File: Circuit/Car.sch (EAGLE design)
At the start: 16 parts, among them M1 MOTOR, M2 MOTOR, U1 AMS1117-3.3, X2 ESP-12

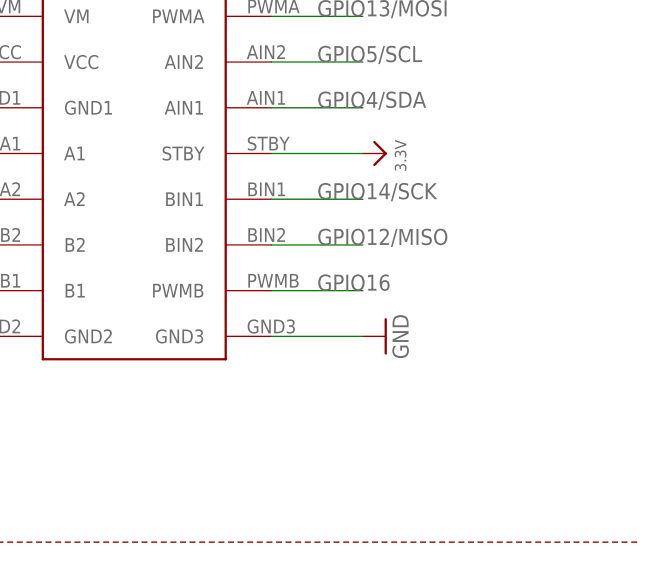
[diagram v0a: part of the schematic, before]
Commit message: Use one output for both pwms
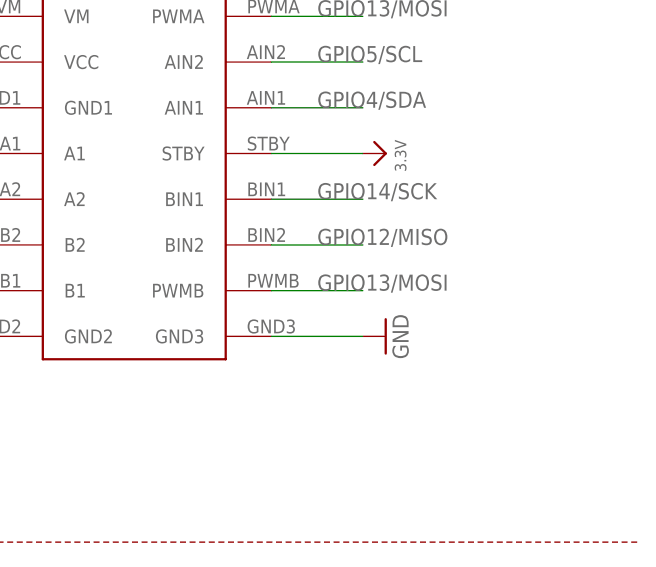
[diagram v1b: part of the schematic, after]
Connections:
- net GPIO13/MOSI: now also TB1.PWMB
- net GPIO16: no longer TB1.PWMB
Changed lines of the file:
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@@
 <label x="15.24" y="81.28" size="1.778" layer="95"/>
-</segment>
-<segment>
-<pinref part="TB1" gate="G$1" pin="PWMB"/>
-<wire x1="215.9" y1="124.46" x2="226.06" y2="124.46" width="0.1524" layer="91"/>
-<label x="220.98" y="124.46" size="1.778" layer="95"/>
 </segment>
 </net>
@@
 <label x="220.98" y="154.94" size="1.778" layer="95"/>
 </segment>
+<segment>
+<pinref part="TB1" gate="G$1" pin="PWMB"/>
+<wire x1="215.9" y1="124.46" x2="226.06" y2="124.46" width="0.1524" layer="91"/>
+<label x="220.98" y="124.46" size="1.778" layer="95"/>
+</segment>
 </net>

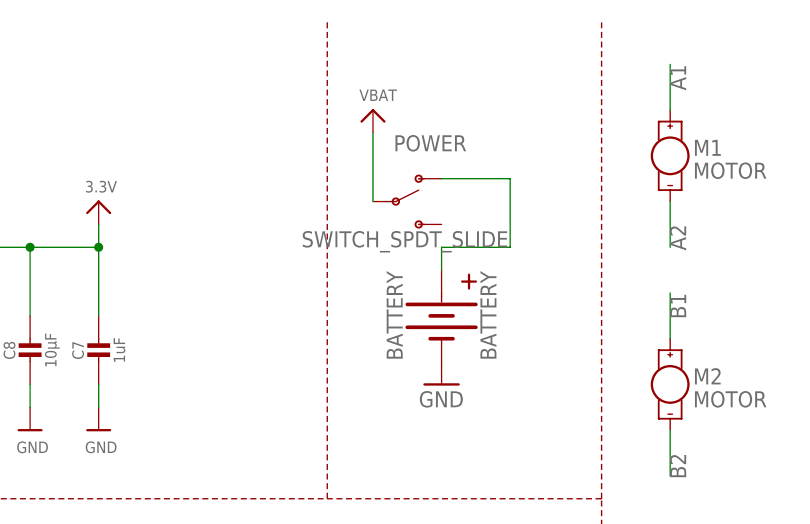
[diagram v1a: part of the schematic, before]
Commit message: update library, car PCB V2
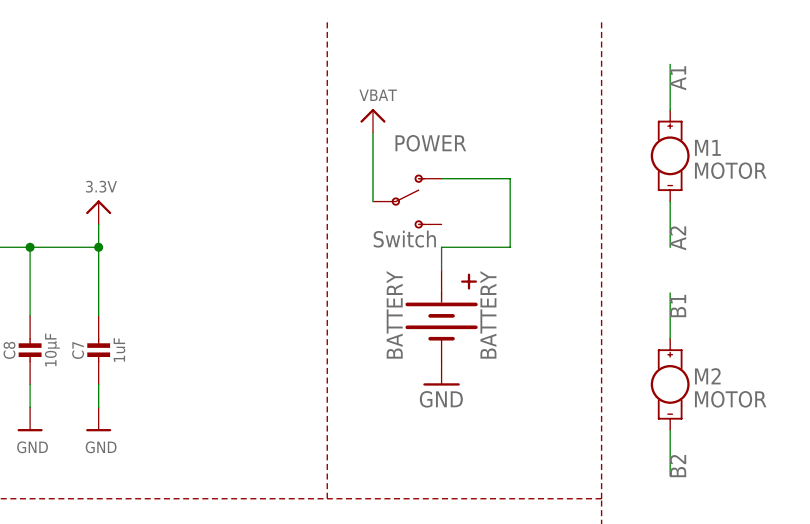
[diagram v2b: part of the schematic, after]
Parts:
- C6, C8: device microbuilder:CAP_CERAMIC0805-NOOUTLINE -> AutoPark:MICROBUILDER_CAP_CERAMIC_0805
- C7: device microbuilder:CAP_CERAMIC0603_NO -> AutoPark:MICROBUILDER_CAP_CERAMIC_0603
- POWER: value SWITCH_SPDT_SLIDE -> Switch
- RN1: device AutoPark:CAY16-750J4LF -> AutoPark:RESISTOR_ARRAY_1206
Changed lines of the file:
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@@
 <layers>
 <layer number="1" name="Top" color="4" fill="1" visible="no" active="no"/>
-<layer number="2" name="Route2" color="1" fill="3" visible="no" active="no"/>
-<layer number="3" name="Route3" color="4" fill="3" visible="no" active="no"/>
-<layer number="4" name="Route4" color="1" fill="4" visible="no" active="no"/>
-<layer number="5" name="Route5" color="4" fill="4" visible="no" active="no"/>
-<layer number="6" name="Route6" color="1" fill="8" visible="no" active="no"/>
-<layer number="7" name="Route7" color="4" fill="8" visible="no" active="no"/>
-<layer number="8" name="Route8" color="1" fill="2" visible="no" active="no"/>
-<layer number="9" name="Route9" color="4" fill="2" visible="no" active="no"/>
-<layer number="10" name="Route10" color="1" fill="7" visible="no" active="no"/>
-<layer number="11" name="Route11" color="4" fill="7" visible="no" active="no"/>
-<layer number="12" name="Route12" color="1" fill="5" visible="no" active="no"/>
-<layer number="13" name="Route13" color="4" fill="5" visible="no" active="no"/>
-<layer number="14" name="Route14" color="1" fill="6" visible="no" active="no"/>
-<layer number="15" name="Route15" color="4" fill="6" visible="no" active="no"/>
+<layer number="2" name="Route2" color="16" fill="1" visible="no" active="no"/>
+<layer number="3" name="Route3" color="17" fill="1" visible="no" active="no"/>
+<layer number="4" name="Route4" color="18" fill="1" visible="no" active="no"/>
+<layer number="5" name="Route5" color="19" fill="1" visible="no" active="no"/>
+<layer number="6" name="Route6" color="25" fill="1" visible="no" active="no"/>
+<layer number="7" name="Route7" color="26" fill="1" visible="no" active="no"/>
+<layer number="8" name="Route8" color="27" fill="1" visible="no" active="no"/>
+<layer number="9" name="Route9" color="28" fill="1" visible="no" active="no"/>
+<layer number="10" name="Route10" color="29" fill="1" visible="no" active="no"/>
+<layer number="11" name="Route11" color="30" fill="1" visible="no" active="no"/>
+<layer number="12" name="Route12" color="20" fill="1" visible="no" active="no"/>
+<layer number="13" name="Route13" color="21" fill="1" visible="no" active="no"/>
+<layer number="14" name="Route14" color="22" fill="1" visible="no" active="no"/>
+<layer number="15" name="Route15" color="23" fill="1" visible="no" active="no"/>
 <layer number="16" name="Bottom" color="1" fill="1" visible="no" active="no"/>
 <layer number="17" name="Pads" color="2" fill="1" visible="no" active="no"/>
 <layer number="18" name="Vias" color="2" fill="1" visible="no" active="no"/>
 <layer number="19" name="Unrouted" color="6" fill="1" visible="no" active="no"/>
-<layer number="20" name="Dimension" color="15" fill="1" visible="no" active="no"/>
-<layer number="21" name="tPlace" color="14" fill="1" visible="no" active="no"/>
-<layer number="22" name="bPlace" color="13" fill="1" visible="no" active="no"/>
-<layer number="23" name="tOrigins" color="14" fill="1" visible="no" active="no"/>
-<layer number="24" name="bOrigins" color="13" fill="1" visible="no" active="no"/>
+<layer number="20" name="Dimension" color="24" fill="1" visible="no" active="no"/>
+<layer number="21" name="tPlace" color="7" fill="1" visible="no" active="no"/>
+<layer number="22" name="bPlace" color="7" fill="1" visible="no" active="no"/>
+<layer number="23" name="tOrigins" color="15" fill="1" visible="no" active="no"/>
+<layer number="24" name="bOrigins" color="15" fill="1" visible="no" active="no"/>
 <layer number="25" name="tNames" color="7" fill="1" visible="no" active="no"/>
 <layer number="26" name="bNames" color="7" fill="1" visible="no" active="no"/>
-<layer number="27" name="tValues" color="11" fill="1" visible="no" active="no"/>
+<layer number="27" name="tValues" color="7" fill="1" visible="no" active="no"/>
 <layer number="28" name="bValues" color="7" fill="1" visible="no" active="no"/>
 <layer number="29" name="tStop" color="7" fill="3" visible="no" active="no"/>
@@
 <parts>
 <part name="FRAME1" library="microbuilder" deviceset="FRAME_A4" device=""/>
-<part name="C6" library="microbuilder" deviceset="CAP_CERAMIC" device="0805-NOOUTLINE" value="10µF"/>
-<part name="C7" library="microbuilder" deviceset="CAP_CERAMIC" device="0603_NO" value="1uF"/>
+<part name="C6" library="AutoPark" deviceset="MICROBUILDER_CAP_CERAMIC" device="_0805" value="10µF"/>
+<part name="C7" library="AutoPark" deviceset="MICROBUILDER_CAP_CERAMIC" device="_0603" value="1uF"/>
 <part name="U$27" library="microbuilder" deviceset="GND" device=""/>
 <part name="U$28" library="microbuilder" deviceset="GND" device=""/>
-<part name="C8" library="microbuilder" deviceset="CAP_CERAMIC" device="0805-NOOUTLINE" value="10µF"/>
+<part name="C8" library="AutoPark" deviceset="MICROBUILDER_CAP_CERAMIC" device="_0805" value="10µF"/>
 <part name="U$29" library="microbuilder" deviceset="GND" device=""/>
 <part name="U$30" library="microbuilder" deviceset="GND" device=""/>
@@
 <part name="GND1" library="supply1" library_urn="urn:adsk.eagle:library:371" deviceset="GND" device=""/>
 <part name="U$1" library="microbuilder" deviceset="VBAT" device=""/>
-<part name="RN1" library="AutoPark" deviceset="CAY16-750J4LF" device="" value="10K"/>
+<part name="RN1" library="AutoPark" deviceset="RESISTOR_ARRAY_1206" device="" value="10K"/>
 <part name="R2" library="SparkFun-Resistors" library_urn="urn:adsk.eagle:library:532" deviceset="RESISTOR" device="1206" package3d_urn="urn:adsk.eagle:package:39654/1" value="4.7K"/>
 <part name="R1" library="SparkFun-Resistors" library_urn="urn:adsk.eagle:library:532" deviceset="RESISTOR" device="1206" package3d_urn="urn:adsk.eagle:package:39654/1" value="1K"/>
@@
 <part name="U$6" library="microbuilder" deviceset="3.3V" device=""/>
 <part name="U$5" library="microbuilder" deviceset="VBAT" device=""/>
-<part name="POWER" library="AutoPark" deviceset="SWITCH_SPDT_SLIDE" device=""/>
+<part name="POWER" library="AutoPark" deviceset="SWITCH_SPDT_SLIDE" device="" value="Switch"/>
 <part name="TB1" library="AutoPark" deviceset="TB6612FNG" device=""/>
 <part name="GND5" library="supply1" library_urn="urn:adsk.eagle:library:371" deviceset="GND" device=""/>

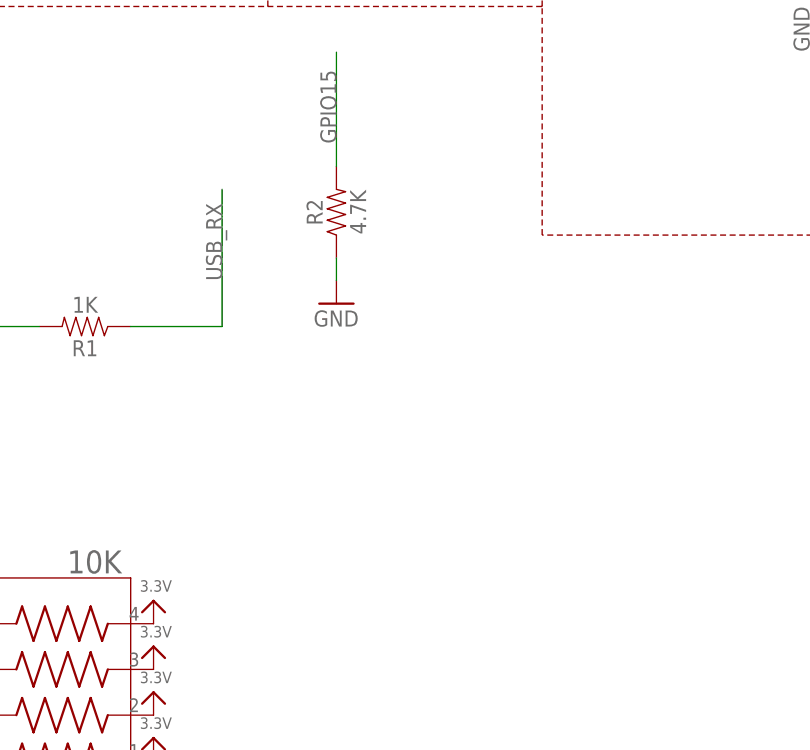
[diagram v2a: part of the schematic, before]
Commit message: car v3 with RGB, update platformio ESP dev structure
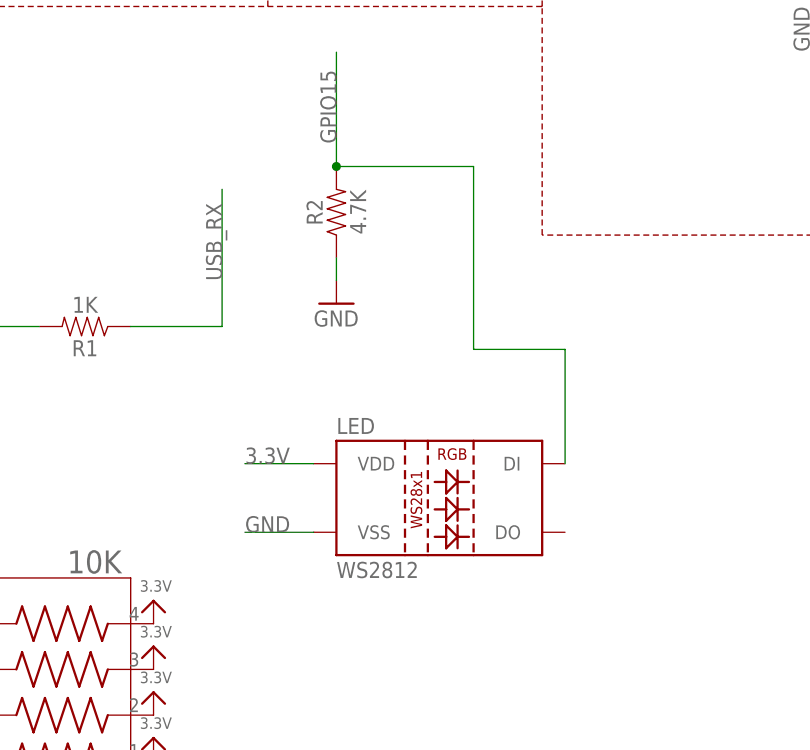
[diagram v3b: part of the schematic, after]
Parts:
- added LED: WS2812, AutoPark:WS2812
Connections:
- net 3.3V: now also LED.VDD
- net GND: now also LED.VSS
- net GPIO15: now also LED.DI
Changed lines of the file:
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@@
 <part name="M1" library="AutoPark" deviceset="MOTOR" device=""/>
 <part name="M2" library="AutoPark" deviceset="MOTOR" device=""/>
+<part name="LED" library="AutoPark" deviceset="WS2812" device="" package3d_urn="urn:adsk.eagle:package:39366/1"/>
 </parts>
 <sheets>
@@
 <attribute name="VALUE" x="152.4" y="132.08" size="1.778" layer="96" font="vector"/>
 </instance>
+<instance part="LED" gate="G$1" x="132.08" y="66.04">
+<attribute name="NAME" x="119.38" y="74.422" size="1.778" layer="95"/>
+<attribute name="VALUE" x="119.38" y="58.42" size="1.778" layer="95"/>
+</instance>
 </instances>
 <busses>
@@
 <wire x1="215.9" y1="119.38" x2="226.06" y2="119.38" width="0.1524" layer="91"/>
 <pinref part="GND8" gate="1" pin="GND"/>
+</segment>
+<segment>
+<pinref part="LED" gate="G$1" pin="VSS"/>
+<wire x1="116.84" y1="63.5" x2="109.22" y2="63.5" width="0.1524" layer="91"/>
+<label x="109.22" y="63.5" size="1.778" layer="95"/>
 </segment>
 </net>
@@
 <pinref part="U$9" gate="G$1" pin="3.3V"/>
 </segment>
+<segment>
+<pinref part="LED" gate="G$1" pin="VDD"/>
+<wire x1="116.84" y1="71.12" x2="109.22" y2="71.12" width="0.1524" layer="91"/>
+<label x="109.22" y="71.12" size="1.778" layer="95"/>
+</segment>
 </net>
 <net name="RESET" class="0">
@@
 <label x="119.38" y="106.68" size="1.778" layer="95" rot="R90"/>
 <pinref part="R2" gate="G$1" pin="2"/>
-</segment>
-</net>
+<wire x1="134.62" y1="104.14" x2="119.38" y2="104.14" width="0.1524" layer="91"/>
+<junction x="119.38" y="104.14"/>
+<wire x1="144.78" y1="83.82" x2="134.62" y2="83.82" width="0.1524" layer="91"/>
+<pinref part="LED" gate="G$1" pin="DI"/>
+<wire x1="144.78" y1="71.12" x2="144.78" y2="83.82" width="0.1524" layer="91"/>
+<wire x1="134.62" y1="83.82" x2="134.62" y2="104.14" width="0.1524" layer="91"/>
+</segment>
+</net>
